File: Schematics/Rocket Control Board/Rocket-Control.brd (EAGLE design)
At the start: 100 x 80 mm, 37 parts

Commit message: Rocket Control Board Work
Significant changes to rocket control board. Too many to detail.
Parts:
- removed U$11, U$12, U$13, U$14, U$15, U$16, U$17, U$18, U$19, U$20, U$23, U$24, U$25, U$27, U$28, U$29, U$30, U$31, U$32, U$33, U$34, U$36, U$37, U$5: HEADER-HOLE, RocketControlBoard:HEADER-HOLE
- added U$38: 10118194-0001LF:MICRO-USB, RocketControlBoard:10118194-0001LF:MICRO-USB-B
- added U$41: SPI-PORT, RocketControlBoard:SPI-PORT
- added U$56: VDDCORE-CAPACITOR, RocketControlBoard:C0603
- added U$57: VIN-CAPACITOR, RocketControlBoard:C0603
- added U$61: JTAG-MINI, RocketControlBoard:JTAG-MINI
- U$21: value HEADER-HOLE -> HEADER-SIDE-A; device RocketControlBoard:HEADER-HOLE -> RocketControlBoard:HEADER-SIDE-A
- U$22: value HEADER-HOLE -> HEADER-SIDE-B; device RocketControlBoard:HEADER-HOLE -> RocketControlBoard:HEADER-SIDE-B
- moved U$22 88.1 mm to (1.27, 36.8), turned to 90 degrees
- moved U$21 73.6 mm to (20.3, 16.5)
- moved U$1 45.2 mm to (12.7, 14.0)
- moved U$10 45.2 mm to (14.0, 5.71)
- moved U$2 45.2 mm to (8.89, 5.71)
- moved U$26 45.2 mm to (16.5, 5.71)
- moved U$3 45.2 mm to (11.4, 5.71)
- moved U$4 45.2 mm to (5.08, 5.71)
- moved U$6 45.2 mm to (14.0, 2.54)
- moved U$7 45.2 mm to (16.5, 2.54)
- moved U$8 45.2 mm to (8.89, 2.54)
- moved U$9 45.2 mm to (11.4, 2.54)
- moved U$35 41.9 mm to (16.5, 21.6), turned to 270 degrees
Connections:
- new net A5: U$1.47, U$21.A5
- new net RX: U$1.38
- new net SWD-06(RESET): U$1.40, U$61.RESET
- new net SWD-09: U$1.45, U$61.JTAG09
- new net SWD-10: U$1.46, U$61.JTAG10
- new net TX: U$1.37
- new net USB: U$22.USB, U$38.1:VBUS
- new net VDDCORE: U$1.43, U$56.1
- new net VIN: U$1.44, U$22.VIN, U$57.1
- net +3V3: now also U$22.3V3, U$41.VIN, U$61.VIN; no longer U$36.P$1
- net A0: now also U$21.A0; no longer U$5.P$1
- net A1: now also U$21.A1; no longer U$11.P$1
- net A2: now also U$21.A2; no longer U$12.P$1
- net A3: now also U$21.A3; no longer U$13.P$1
- net A4: now also U$21.A4; no longer U$14.P$1
- net AREF: now also U$21.AREF
- net D0-TX: now also U$21.D0; no longer U$18.P$1
- net D1-RX: now also U$21.D1; no longer U$17.P$1
- net D10: now also U$22.D10; no longer U$30.P$1
- net D11: now also U$22.D11; no longer U$32.P$1
- net D12: now also U$22.D12; no longer U$29.P$1
- net D13: now also U$22.D13; no longer U$31.P$1
- net D2: now also U$21.D2; no longer U$20.P$1
- net D3: now also U$21.D3; no longer U$19.P$1
- net D4: now also U$21.D4; no longer U$24.P$1
- net D5: now also U$21.D5; no longer U$25.P$1
- net D6: now also U$21.D6; no longer U$28.P$1
- net D7: now also U$22.D7, U$41.ATN; no longer U$27.P$1
- net D8: now also U$22.D8; no longer U$15.P$1
- net D9: now also U$22.D9; no longer U$16.P$1
- net GND: now also U$1.42, U$22.GND-IN, U$22.GND-OUT, U$38.5:GND, U$41.GND, U$56.2, U$57.2, U$61.GND-1, U$61.GND-2, U$61.GND-3; no longer U$37.P$1
- net MISO: now also U$41.MISO; no longer U$23.P$1
- net MOSI: now also U$41.MOSI; no longer U$21.P$1
- net SCK: now also U$41.SCK; no longer U$22.P$1
- net SCL: now also U$22.SCL; no longer U$34.P$1
- net SDA: now also U$22.SDA; no longer U$33.P$1
- net USB-N: now also U$38.2:D-
- net USB-P: now also U$38.3:D+
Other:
- board size 100 x 80 mm -> 21.9 x 35.5 mm

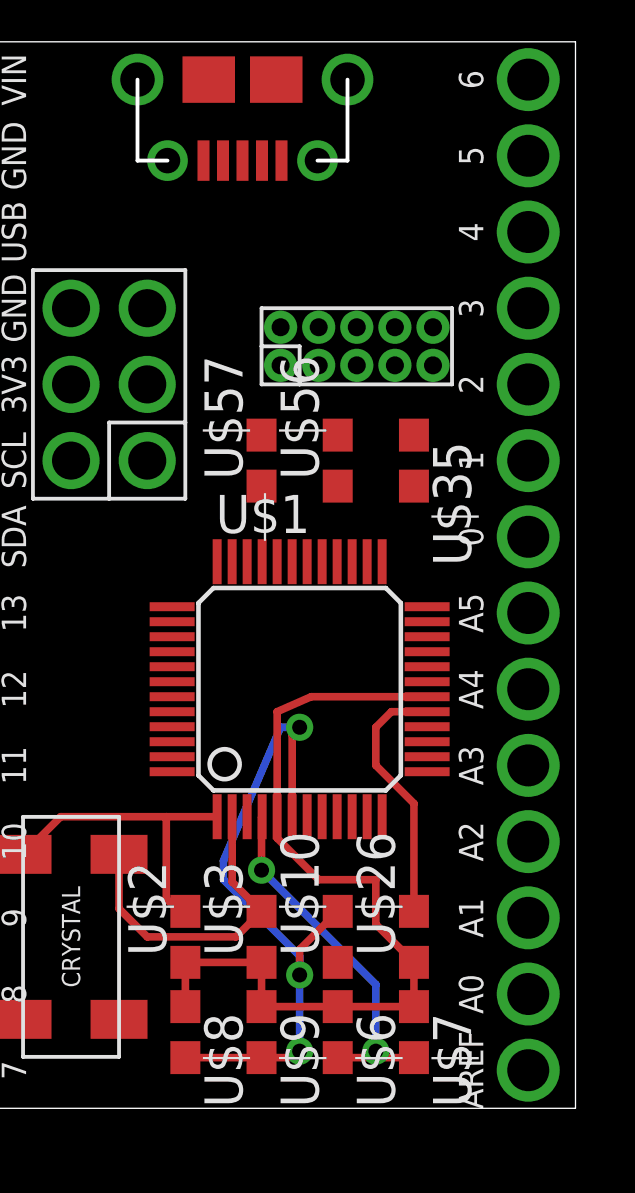
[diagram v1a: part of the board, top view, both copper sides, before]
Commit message: Added Regulator Part
See Title
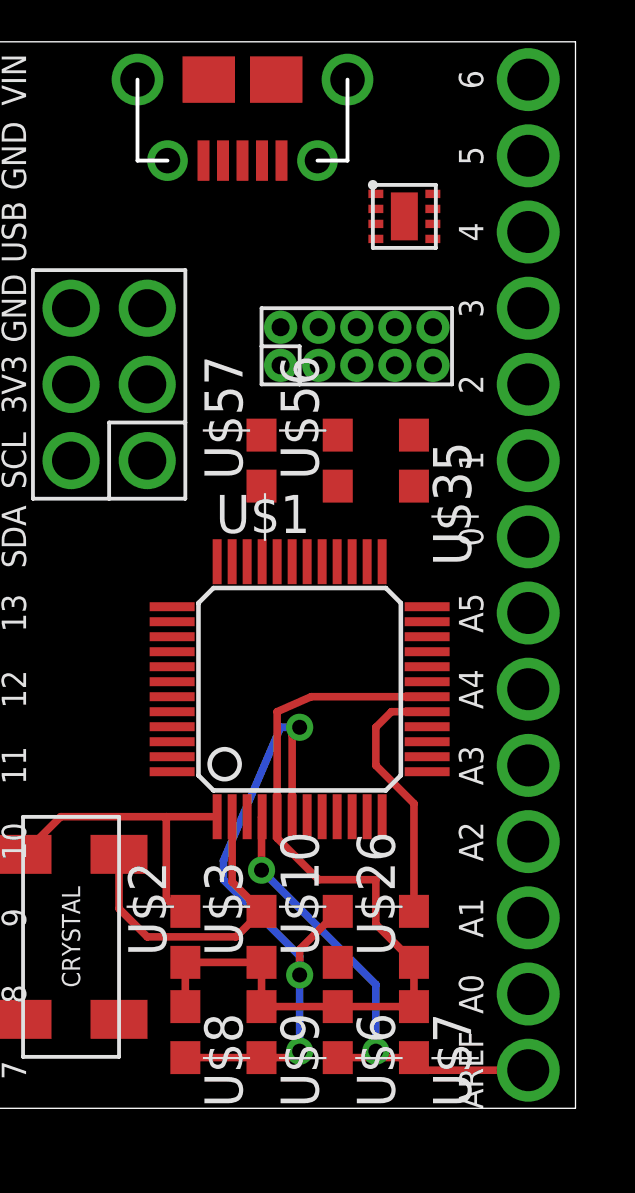
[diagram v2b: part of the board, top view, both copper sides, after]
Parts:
- added U$5: REGULATOR, RocketControlBoard:8-WFDFN-EXPOSED-PAD
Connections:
- new net VIN-REGULATED: U$1.44, U$57.1
- net VIN: no longer U$1.44, U$57.1
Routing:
- net AREF: track 12.1 -> 16.3 mm
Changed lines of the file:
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@@
 <element name="U$21" library="RocketControlBoard" package="HEADER-SIDE-A" value="HEADER-SIDE-A" x="20.32" y="16.51"/>
 <element name="U$22" library="RocketControlBoard" package="HEADER-SIDE-B" value="HEADER-SIDE-B" x="1.27" y="36.83" rot="R90"/>
+<element name="U$5" library="RocketControlBoard" package="8-WFDFN-EXPOSED-PAD" value="REGULATOR" x="15.24" y="30.48" rot="R270"/>
 </elements>
 <signals>
@@
 <wire x1="15.455" y1="1.69" x2="15.24" y2="1.905" width="0.254" layer="1"/>
 <contactref element="U$21" pad="AREF"/>
-<wire x1="16.51" y1="1.69" x2="20.32" y2="1.27" width="0" layer="19" extent="1-1"/>
+<wire x1="20.32" y1="1.27" x2="16.51" y2="1.27" width="0.254" layer="1"/>
+<wire x1="16.51" y1="1.27" x2="16.51" y2="1.69" width="0.254" layer="1"/>
 </signal>
 <signal name="+3V3">
@@
 </signal>
 <signal name="VIN">
-<contactref element="U$1" pad="44"/>
-<contactref element="U$57" pad="1"/>
 <contactref element="U$22" pad="VIN"/>
-<wire x1="11.43" y1="20.74" x2="1.27" y2="34.29" width="0" layer="19" extent="1-1"/>
-<wire x1="8.45" y1="13.22" x2="11.43" y2="20.74" width="0" layer="19" extent="1-1"/>
 </signal>
 <signal name="A5">
@@
 <contactref element="U$1" pad="37"/>
 </signal>
+<signal name="VIN-REGULATED">
+<contactref element="U$1" pad="44"/>
+<contactref element="U$57" pad="1"/>
+<wire x1="8.45" y1="13.22" x2="11.43" y2="20.74" width="0" layer="19" extent="1-1"/>
+</signal>
 </signals>

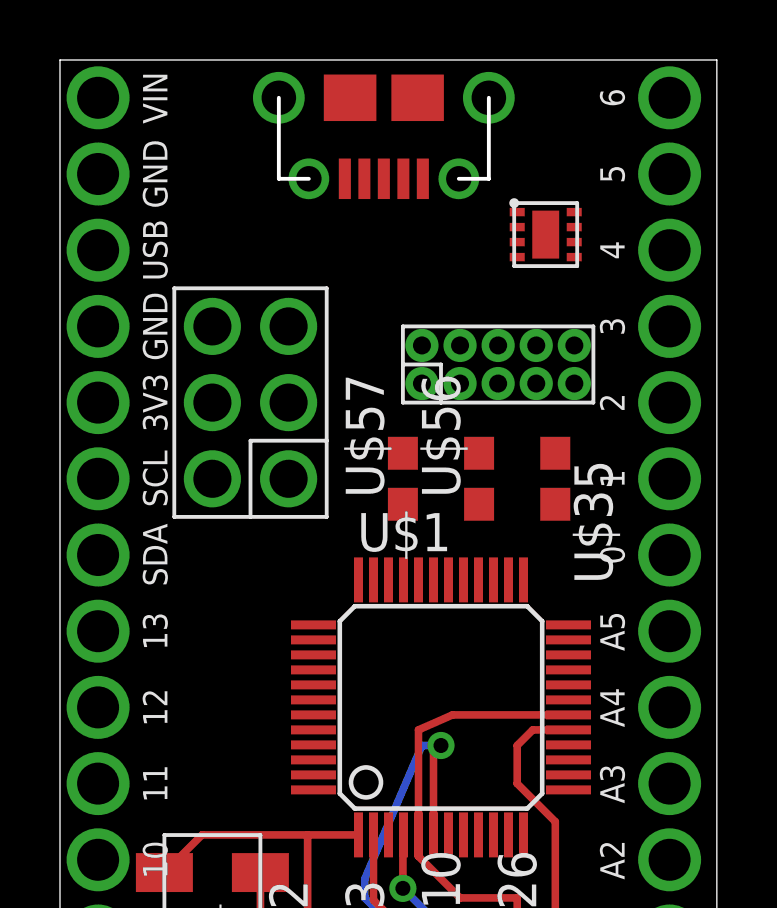
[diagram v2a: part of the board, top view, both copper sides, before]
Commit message: Added regulator and supporting components
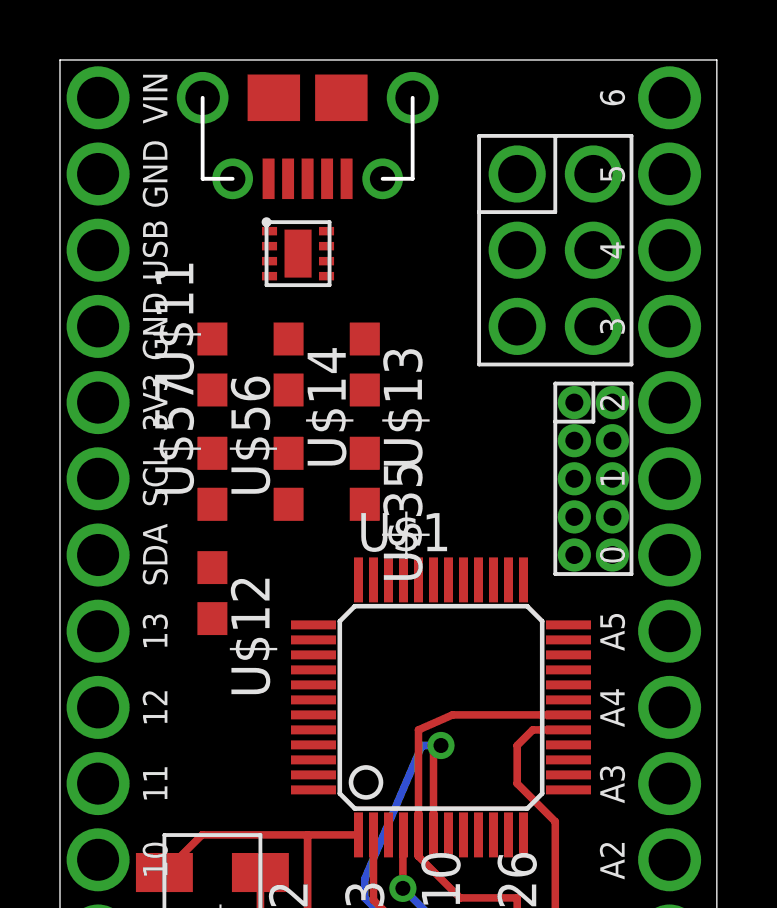
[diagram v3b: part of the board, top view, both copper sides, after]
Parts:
- added U$11, U$12: REGULATOR-CAPACITORS, RocketControlBoard:C0603
- added U$13: REGULATOR-INDUCTOR, RocketControlBoard:C0603
- added U$14: REGULATOR-RESISTOR, RocketControlBoard:C0603
- moved U$5 8.28 mm to (6.99, 29.8)
- moved U$41 7.62 mm to (15.2, 26.7), turned to 0 degrees
- moved U$35 6.35 mm to (10.2, 21.6)
- moved U$56 6.35 mm to (7.62, 21.6)
- moved U$57 6.35 mm to (5.08, 21.6)
- moved U$61 5.85 mm to (16.5, 18.4), turned to 0 degrees
- moved U$38 2.54 mm to (8.26, 34.3)
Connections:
- new net N$1: U$13.1, U$5.PG
- new net N$3: U$14.1, U$5.VOS
- net GND: now also U$11.1, U$12.1, U$5.AGND, U$5.EN, U$5.EXPOSED-THERMAL-PAD, U$5.FB
- net VIN: now also U$11.2, U$5.PGND, U$5.VIN
- net VIN-REGULATED: now also U$12.2, U$13.2, U$14.2, U$5.SW
